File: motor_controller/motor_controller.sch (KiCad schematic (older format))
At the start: 21 parts, among them J101 Conn_01x06, J102 Conn_01x06, J103 Barrel_Jack_Switch, J104 Conn_01x06, J105 Conn_01x08, J106 Conn_01x06, J107 Conn_01x10, J108 Conn_01x08, U101 MAX14780, U102 MAX14780

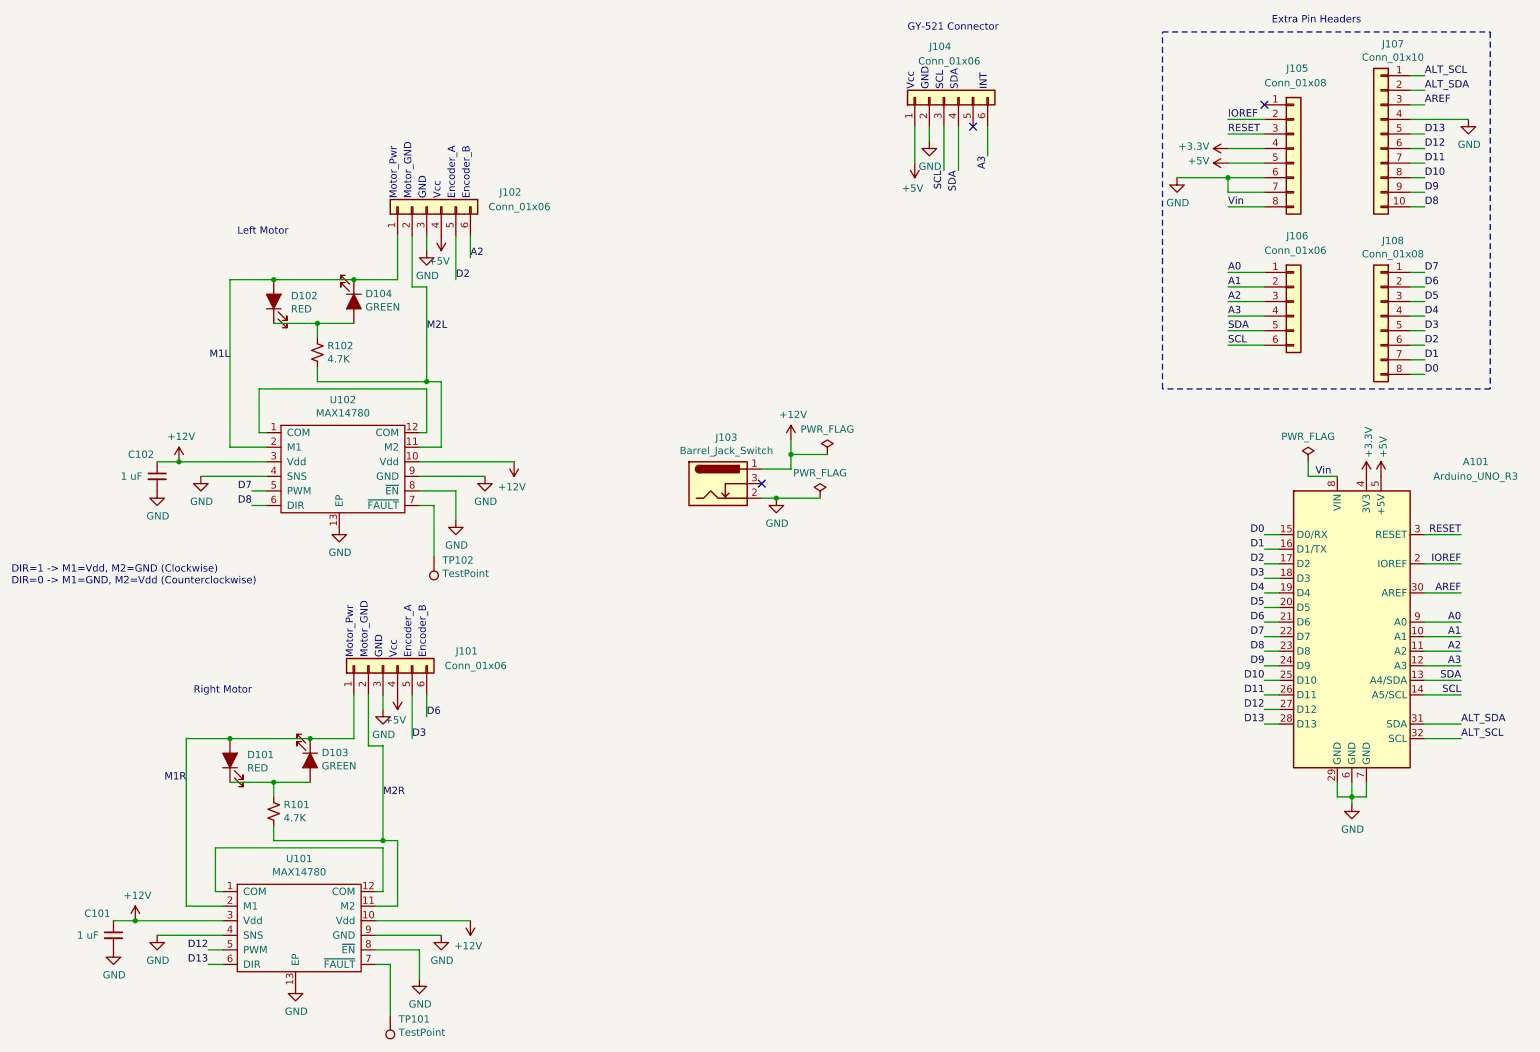
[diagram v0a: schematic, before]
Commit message: updated schematic pdf and generated gerber files
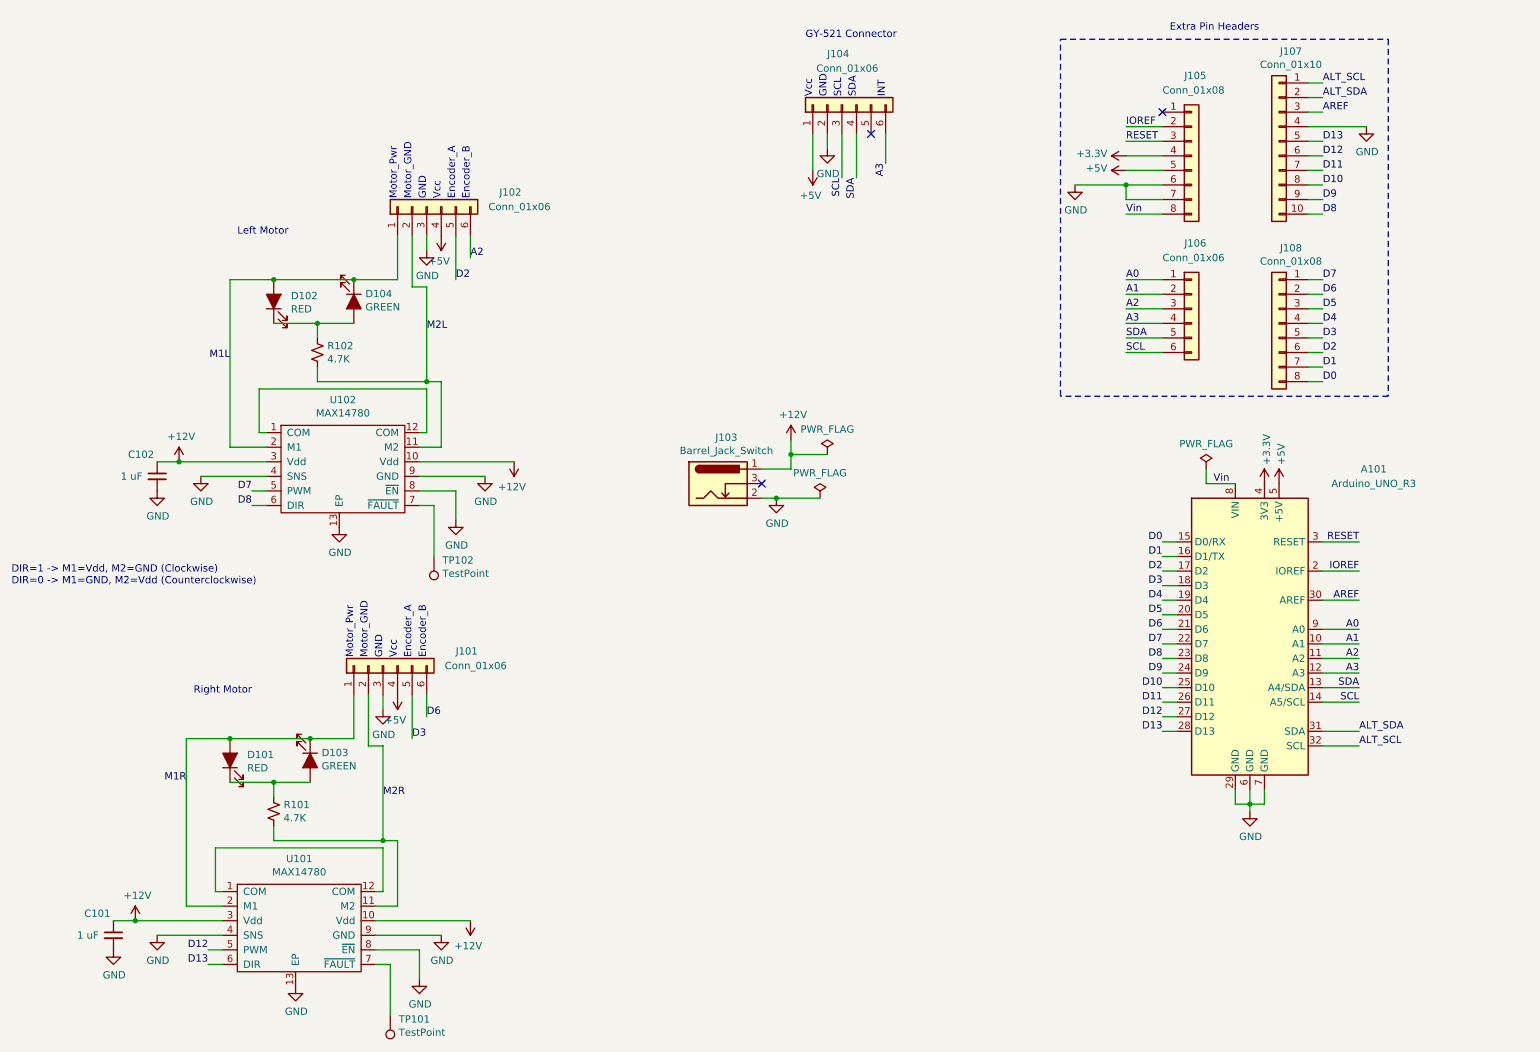
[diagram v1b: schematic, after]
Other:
- moved on the sheet: A101, J104, J105, J106, J107, J108
